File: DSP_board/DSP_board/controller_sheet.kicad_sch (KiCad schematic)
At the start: 5 parts, among them IC1 74LCX125MTCX, IC2 74LCX125MTCX, IC3 74LCX125MTCX, IC4 74LCX125MTCX, U1 AM264LAUNCH

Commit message: including FPGA
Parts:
- removed IC1, IC2, IC3, IC4: 74LCX125MTCX, SOP65P640X120-14N, symbol 74125:74LCX125MTCX
- removed U1: AM264LAUNCH, am263x_devboard:AM2634_LAUNCH, symbol am264xlaunchpad:AM264LAUNCH
- added B1: Arty-S7, Connector_PinHeader_2.54mm:Arty-S7, symbol Connector:Arty-S7
- added C16, C17: 10u, Capacitor_SMD:C_0603_1608Metric_Pad1.08x0.95mm_HandSolder, symbol pspice:CAP
- added C18: 2.2u, Capacitor_SMD:C_0603_1608Metric_Pad1.08x0.95mm_HandSolder, symbol pspice:CAP
- added Cvdd_1, Cvdd_2, Cvdd_3, Cvdd_4, Cvdda_1, Cvdda_2, Cvddio_1, Cvddio_2, Cvddio_3, Cvddio_4: 0.1u, Capacitor_SMD:C_0603_1608Metric_Pad1.08x0.95mm_HandSolder, symbol pspice:CAP
- added FB1: BKP1005HS221-T, BKP100:BEADC1005X55N, symbol BK100:BKP1005HS221-T
- added FB2: MPZ1005S600CT000, BKP100:BEADC1005X55N, symbol MPZ100:MPZ1005S600CT000
- added IC5: F280025CPNQR, f280025c:f280025c, symbol f280025C:F280025CPNQR
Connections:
- net DAB1PWM11: now also B1.69 (JA10)
- net DAB1PWM12: now also B1.68 (JA9)
- net DAB1PWM21: now also B1.67 (JA8)
- net DAB1PWM22: now also B1.66 (JA7)
- net DAB2_PWM11: now also B1.81 (JB10)
- net DAB2_PWM12: now also B1.80 (JB9)
- net DAB2_PWM21: now also B1.79 (JB8)
- net DAB2_PWM22: now also B1.78 (JB7)
- net I_leackage: now also IC5.18 (A1)
- net Igrid1_sense: now also IC5.14 (A15C7)
- net Igrid2_sense: now also IC5.12 (A3C5)
- net Igrid3_sense: now also IC5.10 (A6)
- net VSI11: now also B1.102 (JD7)
- net VSI12: now also B1.103 (JD8)
- net VSI21: now also B1.104 (JD9)
- net VSI22: now also B1.105 (JD10)
- net VSI31: now also B1.98 (JD3)
- net VSI32: now also B1.99 (JD4)
- net Vdc_link: now also IC5.22 (A12C1)
- net Vgrid1_sense: now also IC5.15 (A14C4)
- net Vgrid2_sense: now also IC5.13 (A2C9)
- net Vgrid3_sense: now also IC5.11 (C6)
- net batt_V_sense: now also IC5.17 (A5C2)
- net batt_curr_sense: now also IC5.16 (A11C0)
- new net VDD: C17.1, Cvdd_1.1, Cvdd_2.1, Cvdd_3.1, Cvdd_4.1, IC5.31 (VDD_2), IC5.53 (VDD_3), IC5.71 (VDD_4), IC5.8 (VDD_1)
- new net VDDA: Cvdda_1.1, Cvdda_2.1, FB2.1, IC5.26 (VDDA)
- new net VDDIO: Cvddio_1.1, Cvddio_2.1, Cvddio_3.1, Cvddio_4.1, FB1.1, IC5.32 (VDDIO_2), IC5.52 (VDDIO_3), IC5.7 (VDDIO_1), IC5.72 (VDDIO_4)
- new net ctrl_3v3: C16.1, C18.1, FB1.2, FB2.2
- new net ctrl_gnd: C16.2, C17.2, C18.2, Cvdd_1.2, Cvdd_2.2, Cvdd_3.2, Cvdd_4.2, Cvdda_1.2, Cvdda_2.2, Cvddio_1.2, Cvddio_2.2, Cvddio_3.2, Cvddio_4.2, IC5.25 (VSSA), IC5.30 (VSS_2), IC5.55 (VSS_3), IC5.70 (VSS_4), IC5.9 (VSS_1)
- new net pwmVSI1: B1.59 (IO0), IC5.63 (GPIO0)
- new net pwmVSI2: B1.58 (IO1), IC5.61 (GPIO2)
- new net pwmVSI3: B1.57 (IO2), IC5.59 (GPIO4)
- new net pwm_daba1: B1.56 (IO3), IC5.80 (GPIO6)
- new net pwm_daba2: B1.55 (IO4), IC5.58 (GPIO8)
- new net pwm_dabb1: B1.54 (IO5), IC5.76 (GPIO10)
- new net pwm_dabb2: B1.53 (IO6), IC5.36 (GPIO12)
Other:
- note added: "Each capacitor is at each VDD pin and connected to ground, all VDD pins are also shorted to each other"
- note added: "Each capacitor is at each VDDIO pin and connected to ground, all VDDIO pins are also shorted to each other"
- note added: "place near VDDA pin directly connected to it"

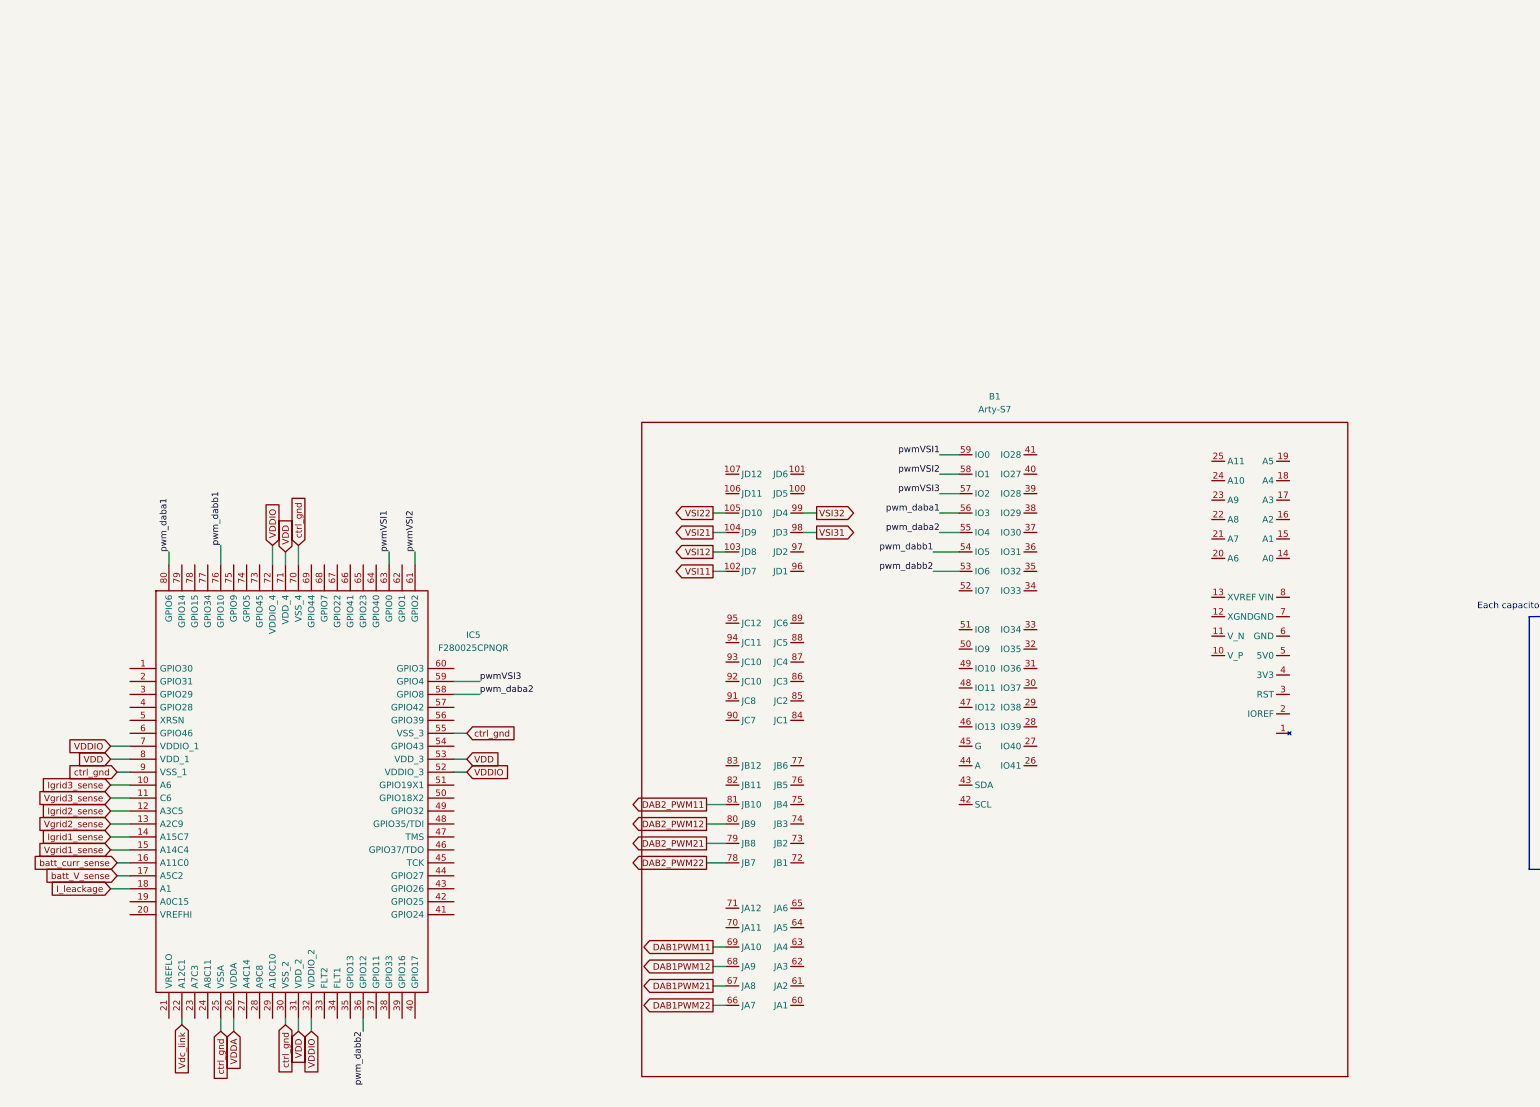
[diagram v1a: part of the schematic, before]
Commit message: Connecting FPGA ADC pins
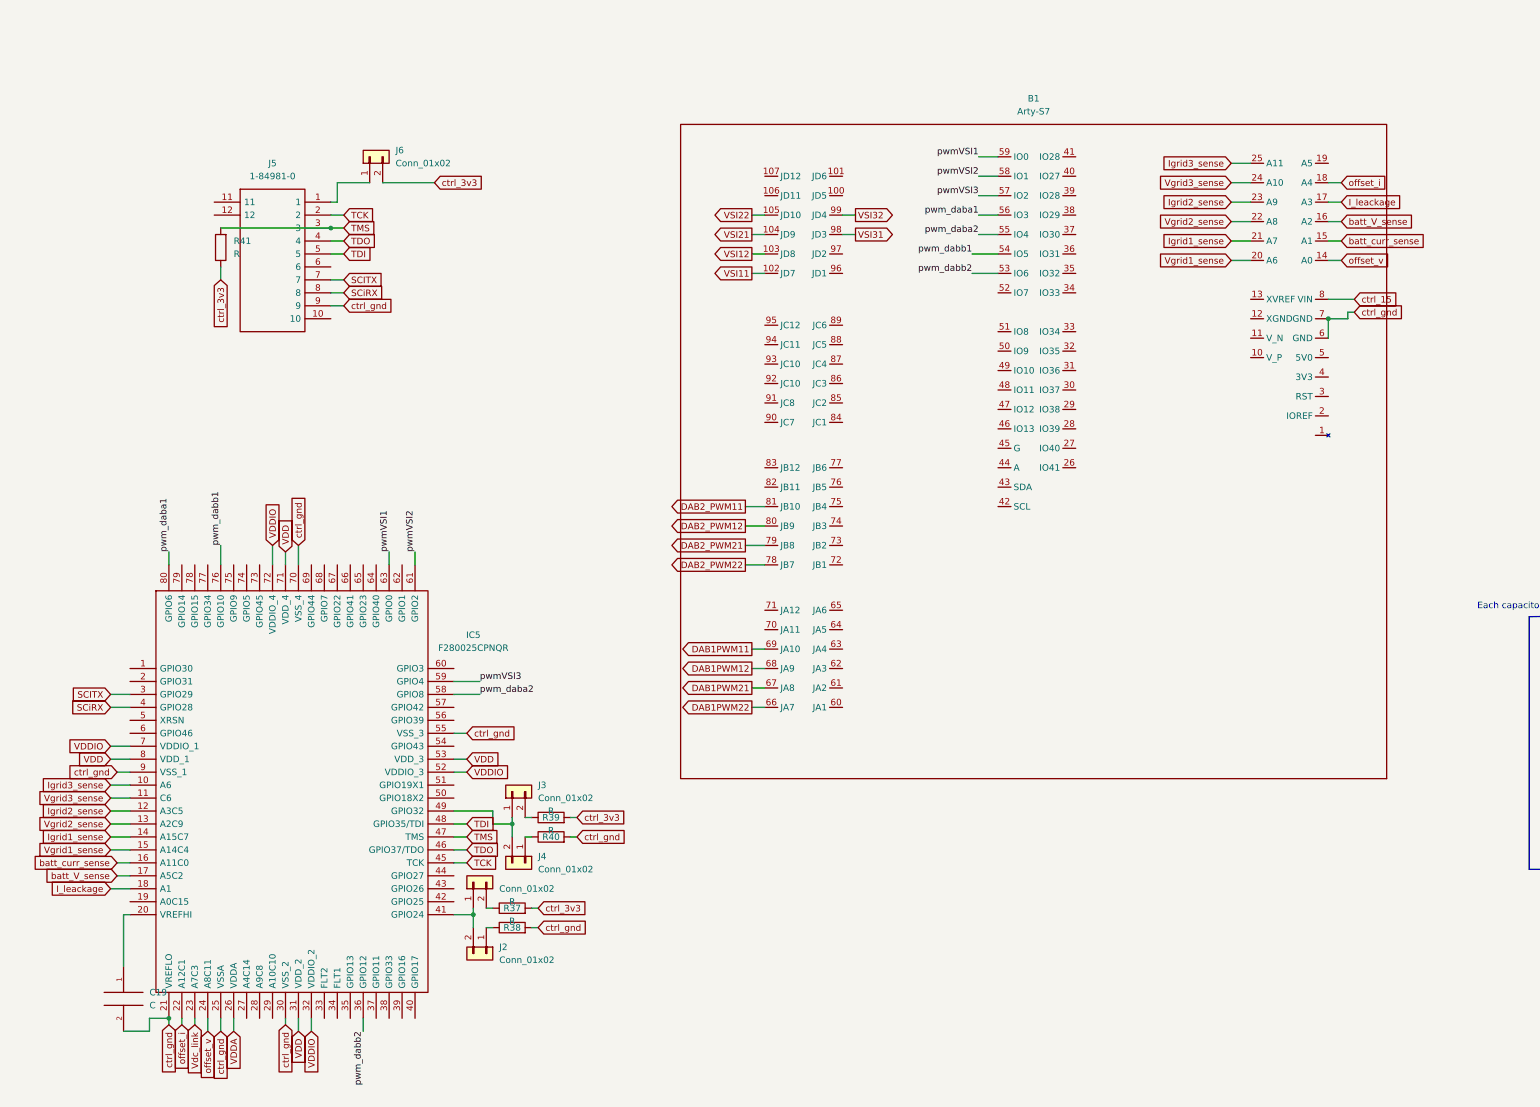
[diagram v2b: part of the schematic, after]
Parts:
- added C19: C, Capacitor_SMD:C_0805_2012Metric_Pad1.18x1.45mm_HandSolder, symbol pspice:C
- added J1, J2, J3, J4, J6: Conn_01x02, Connector_PinHeader_2.54mm:PinHeader_1x02_P2.54mm_Vertical, symbol Connector_Generic:Conn_01x02
- added J5: 1-84981-0, jtag_connector:1849810, symbol ribbon_connector:1-84981-0
- added R37, R38, R39, R40, R41: R, Resistor_SMD:R_1206_3216Metric_Pad1.30x1.75mm_HandSolder, symbol Device:R
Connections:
- net I_leackage: now also B1.17 (A3)
- net Igrid1_sense: now also B1.21 (A7)
- net Igrid2_sense: now also B1.23 (A9)
- net Igrid3_sense: now also B1.25 (A11)
- net Vdc_link: now also IC5.23 (A7C3); no longer IC5.22 (A12C1)
- net Vgrid1_sense: now also B1.20 (A6)
- net Vgrid2_sense: now also B1.22 (A8)
- net Vgrid3_sense: now also B1.24 (A10)
- net batt_V_sense: now also B1.16 (A2)
- net batt_curr_sense: now also B1.15 (A1)
- net ctrl_3v3: now also J6.2 (Pin_2), R37.2, R39.2, R41.1
- net ctrl_gnd: now also B1.6 (GND), B1.7 (GND), IC5.21 (VREFLO), C19.2, J5.9, R38.2, R40.2
- net at IC5.20 (VREFHI): now also C19.1
- net offset_v: now reaches IC5.24 (A8C11)
- net offset_v: now also B1.14 (A0)
- net SCITX: now reaches IC5.3 (GPIO29)
- net SCITX: now also J5.7
- net SCiRX: now reaches IC5.4 (GPIO28)
- net SCiRX: now also J5.8
- net at IC5.41 (GPIO24): now also J1.1 (Pin_1), J2.2 (Pin_2)
- net TCK: now reaches IC5.45 (TCK)
- net TCK: now also J5.2
- net TDO: now reaches IC5.46 (GPIO37/TDO)
- net TDO: now also J5.4
- net TMS: now reaches IC5.47 (TMS)
- net TMS: now also J5.3, R41.2
- net TDI: now reaches IC5.48 (GPIO35/TDI)
- net TDI: now also J5.5
- net at IC5.49 (GPIO32): now also J3.1 (Pin_1), J4.2 (Pin_2)
- net offset_i: now reaches B1.18 (A4)
- net offset_i: now also IC5.22 (A12C1)
- net ctrl_15: now reaches B1.8 (VIN)
- new net: J4.1 (Pin_1), R40.1
- new net: J5.1, J6.1 (Pin_1)
- new net: J3.2 (Pin_2), R39.1
- new net: J1.2 (Pin_2), R37.1
- new net: J2.1 (Pin_1), R38.1
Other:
- moved on the sheet: B1

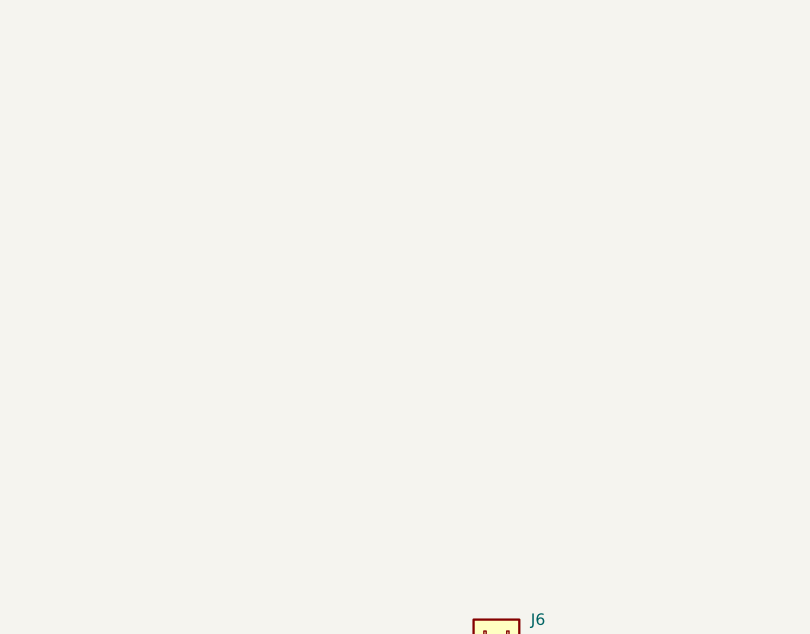
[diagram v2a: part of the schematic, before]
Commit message: introduce diode
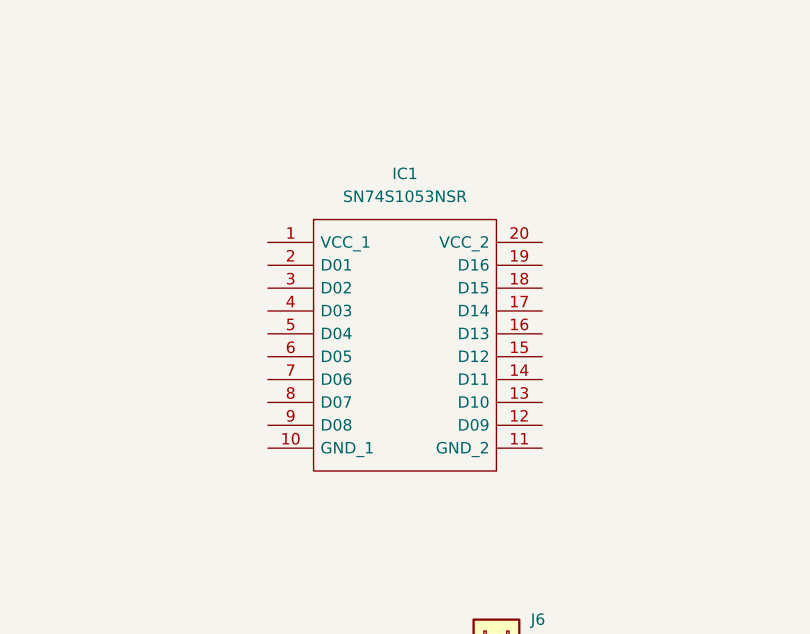
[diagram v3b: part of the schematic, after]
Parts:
- added IC1: SN74S1053NSR, sn74s:sn74, symbol diode_adc:SN74S1053NSR
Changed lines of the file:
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@@
     (pin "2")
+  )
+  (symbol (lib_id "diode_adc:SN74S1053NSR") (at 55.88 59.69 0) (unit 1)
+    (in_bom yes) (on_board yes) (fields_autoplaced)
+    (property "Reference" "IC1" (id 0) (at 71.12 52.07 0))
+    (property "Value" "SN74S1053NSR" (id 1) (at 71.12 54.61 0))
+    (property "Footprint" "sn74s:sn74" (id 2) (at 82.55 57.15 0)
+      (effects (font (size 1.27 1.27)) (justify left) hide)
+    )
+    (property "Datasheet" "http://www.ti.com/lit/gpn/sn74s1053" (id 3) (at 82.55 59.69 0)
+      (effects (font (size 1.27 1.27)) (justify left) hide)
+    )
+    (property "Description" "16-Bit Schottky Barrier Diode Bus-Termination Array" (id 4) (at 82.55 62.23 0)
+      (effects (font (size 1.27 1.27)) (justify left) hide)
+    )
+    (property "Height" "2" (id 5) (at 82.55 64.77 0)
+      (effects (font (size 1.27 1.27)) (justify left) hide)
+    )
+    (property "Mouser Part Number" "595-SN74S1053NSR" (id 6) (at 82.55 67.31 0)
+      (effects (font (size 1.27 1.27)) (justify left) hide)
+    )
+    (property "Mouser Price/Stock" "https://www.mouser.co.uk/ProductDetail/Texas-Instruments/SN74S1053NSR?qs=gb35HGp1gQKBVeOxZl0Yrw%3D%3D" (id 7) (at 82.55 69.85 0)
+      (effects (font (size 1.27 1.27)) (justify left) hide)
+    )
+    (property "Manufacturer_Name" "Texas Instruments" (id 8) (at 82.55 72.39 0)
+      (effects (font (size 1.27 1.27)) (justify left) hide)
+    )
+    (property "Manufacturer_Part_Number" "SN74S1053NSR" (id 9) (at 82.55 74.93 0)
+      (effects (font (size 1.27 1.27)) (justify left) hide)
+    )
+    (pin "1")
+    (pin "10")
+    (pin "11")
+    (pin "12")
+    (pin "13")
+    (pin "14")
+    (pin "15")
+    (pin "16")
+    (pin "17")
+    (pin "18")
+    (pin "19")
+    (pin "2")
+    (pin "20")
+    (pin "3")
+    (pin "4")
+    (pin "5")
+    (pin "6")
+    (pin "7")
+    (pin "8")
+    (pin "9")
   )
   (symbol (lib_id "Connector_Generic:Conn_01x02") (at 102.87 259.08 270) (unit 1)
